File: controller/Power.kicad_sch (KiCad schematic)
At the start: 8 parts, among them U1 10118194-MICRO-USB, U2 LM3671MF-3.3/NOPBMF05A-M

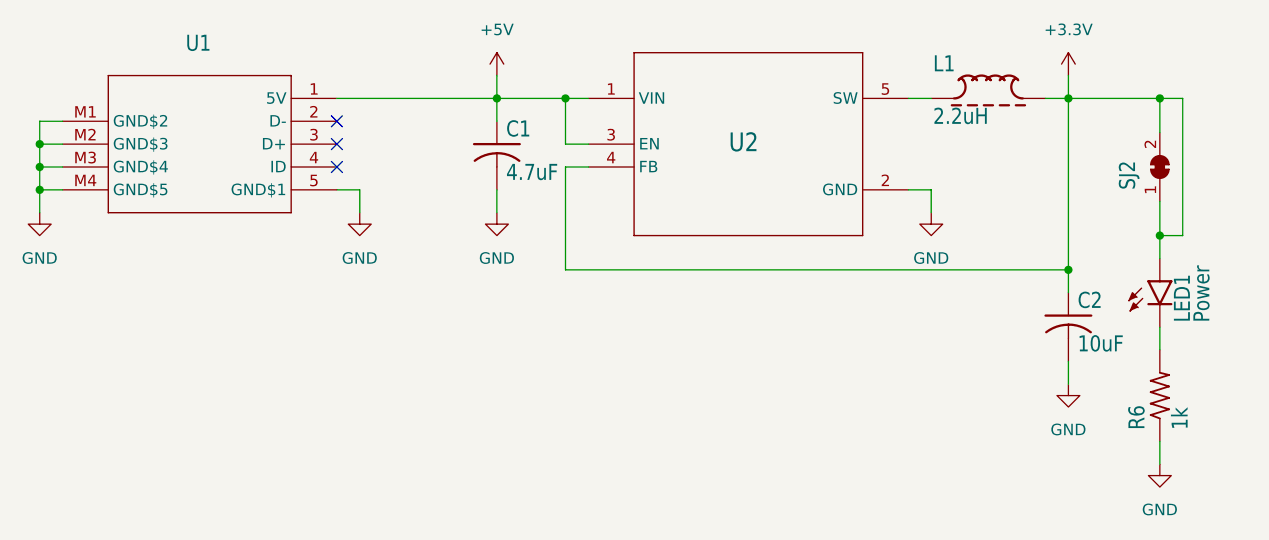
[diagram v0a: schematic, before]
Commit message: Cleaned up controller
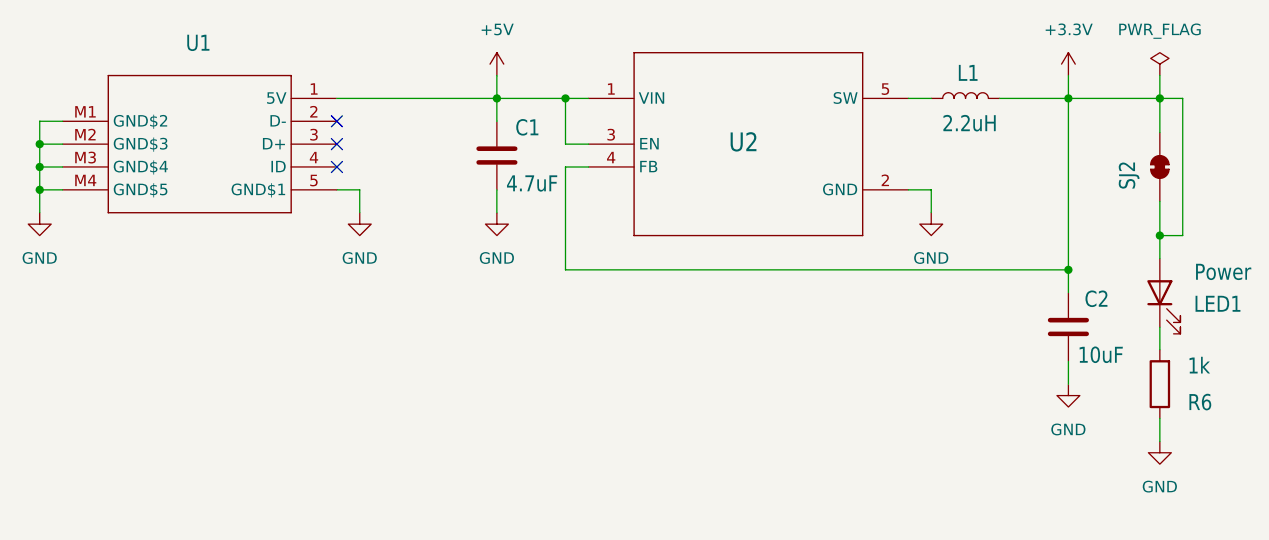
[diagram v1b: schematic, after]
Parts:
- C1, C2: footprint controller:C0805 -> Capacitor_SMD:C_0805_2012Metric_Pad1.18x1.45mm_HandSolder; symbol controller-eagle-import:C-USC0805 -> Device:C
- L1: footprint controller:C0805 -> Inductor_SMD:L_0805_2012Metric_Pad1.05x1.20mm_HandSolder; symbol controller-eagle-import:IND-0805 -> Device:L
- LED1: footprint controller:CHIPLED_0805 -> LED_SMD:LED_0805_2012Metric_Pad1.15x1.40mm_HandSolder; symbol controller-eagle-import:LEDCHIPLED_0805 -> Device:LED
- R6: footprint controller:R0805 -> Resistor_SMD:R_0805_2012Metric_Pad1.20x1.40mm_HandSolder; symbol controller-eagle-import:R-US_R0805 -> Device:R
- SJ2: footprint controller:SJ -> Jumper:SolderJumper-2_P1.3mm_Bridged_RoundedPad1.0x1.5mm
- U1: symbol controller-eagle-import:10118194-MICRO-USB -> controller:10118194-MICRO-USB
- U2: symbol controller-eagle-import:LM3671MF-3.3/NOPBMF05A-M -> controller:LM3671MF-3.3/NOPBMF05A-M
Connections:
- net +3.3V: now also LED1.2 (A); no longer LED1.A
- net at R6.2: now also LED1.1 (K); no longer LED1.C
